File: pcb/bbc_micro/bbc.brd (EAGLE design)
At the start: 43 x 30 mm, 25 parts, among them U2 LM2776

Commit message: minor adjustment before production
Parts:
- moved U$4 6.15 mm to (20.0, 6.15)
- moved U$3 6.12 mm to (7.93, 5.80)
- moved C5 6.08 mm to (29.2, 2.56)
- moved J4 6.08 mm to (26.5, 22.3)
- moved U$5 6.08 mm to (26.3, 13.7)
- moved JP1 6.08 mm to (4.16, 1.83)
- moved C1 6.08 mm to (36.0, 13.1)
- moved C2 6.08 mm to (34.0, 20.3)
- moved C3 6.08 mm to (27.1, 8.65)
- moved C4 6.08 mm to (26.1, 2.56)
- moved C6 6.08 mm to (34.0, 13.1)
- moved C8 6.08 mm to (25.9, 10.7)
- moved C9 6.08 mm to (21.1, 16.4)
- moved JP3 6.08 mm to (33.3, 5.86)
- moved LED3 6.08 mm to (32.0, 13.1)
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
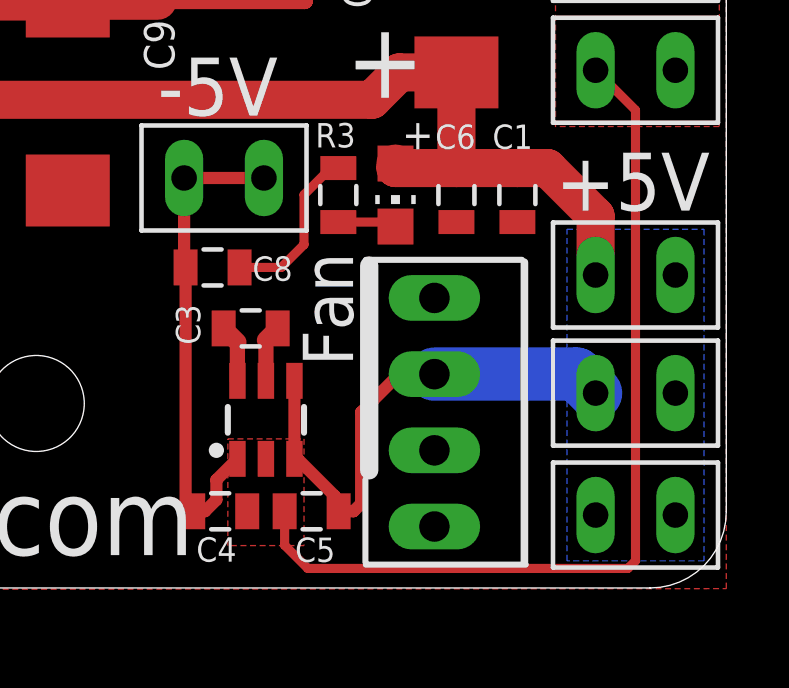
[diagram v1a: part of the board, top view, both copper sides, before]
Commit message: updated fan header
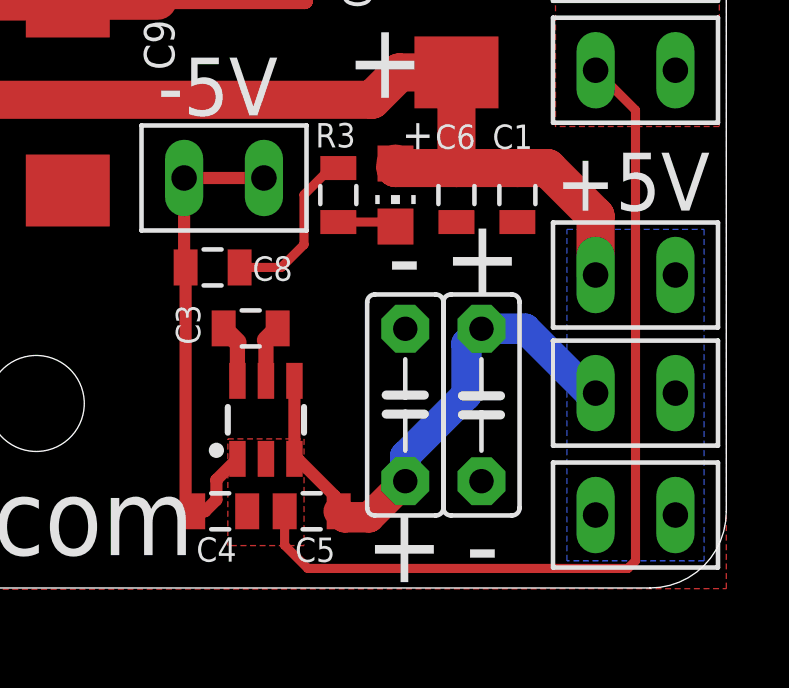
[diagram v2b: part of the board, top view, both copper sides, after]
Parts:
- removed JP3: (no value), appleii:1X04
- added C10, C16: (no value), capacitor-wima:C5B2.5
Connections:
- net +5V: now also C10.1, C16.1; no longer JP3.2
- net GND: now also C10.2, C16.2; no longer JP3.1
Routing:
- net +5V: track 70.0 -> 71.2 mm
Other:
- board text added: "-"
- board text removed: "Fan"
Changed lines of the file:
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@@
 <setting verticaltext="up"/>
 </settings>
-<grid distance="0.1" unitdist="mm" unit="mm" style="lines" multiple="1" display="no" altdistance="1" altunitdist="mil" altunit="mil"/>
+<grid distance="0.1" unitdist="mm" unit="mil" style="lines" multiple="1" display="no" altdistance="1" altunitdist="mil" altunit="mil"/>
 <layers>
 <layer number="1" name="Top" color="4" fill="1" visible="yes" active="yes"/>
@@
 <text x="36.2248" y="25.831" size="1.6764" layer="25" distance="35" rot="R90" align="center">GND</text>
 <rectangle x1="-1.395" y1="27.99" x2="12.605" y2="29.99" layer="51"/>
-<text x="29.721" y="9.287" size="1.6764" layer="25" distance="35" rot="R270" align="center">Fan</text>
 <text x="39.881" y="13.5442" size="1.9304" layer="25" distance="35" align="center">+5V</text>
 <text x="26.049" y="16.7138" size="1.9304" layer="25" distance="35" rot="R180" align="center">-5V</text>
@@
 <text x="31.626" y="17.6082" size="2.54" layer="25" distance="35" align="center">+</text>
 <text x="19.307" y="21.4182" size="2.54" layer="25" distance="35" align="center">+</text>
+<text x="32.271" y="1.465" size="2.54" layer="25" distance="35" align="center">+</text>
+<text x="34.871" y="1.465" size="2.54" layer="25" distance="35" align="center">-</text>
+<text x="34.871" y="11.065" size="2.54" layer="25" distance="35" align="center">+</text>
+<text x="32.271" y="11.065" size="2.54" layer="25" distance="35" align="center">-</text>
 </plain>
 <attributes>
@@
 <element name="U$4" library="a" package="M3_MOUNTING_HOLE_PACK" value="M3_MOUNTING_HOLE" x="20" y="6.15" smashed="yes"/>
 <element name="U$3" library="atx4vc" package="ROCK_SWITCH" value="ROCK_SW" x="7.93" y="5.8" smashed="yes"/>
-<element name="JP3" library="appleii" package="1X04" value="" x="33.271" y="5.858" smashed="yes" rot="R270"/>
 <element name="U$6" library="blade" package="2.8BLADE" value="BLADE28" x="39.974" y="10.432" smashed="yes"/>
 <element name="U$7" library="blade" package="2.8BLADE" value="BLADE28" x="39.974" y="6.495" smashed="yes"/>
@@
 <attribute name="SPICEPREFIX" value="C" x="21.051" y="16.399" size="1.778" layer="27" rot="R270" display="off"/>
 </element>
+<element name="C10" library="capacitor-wima" library_urn="urn:adsk.eagle:library:116" package="C5B2.5" package3d_urn="urn:adsk.eagle:package:5426/1" value="" x="34.84" y="6.1" smashed="yes" rot="R270">
+<attribute name="POPULARITY" value="10" x="34.84" y="6.1" size="1.778" layer="27" rot="R270" display="off"/>
+<attribute name="VALUE" x="32.046" y="8.132" size="1.27" layer="27" ratio="10" rot="R270"/>
+</element>
+<element name="C16" library="capacitor-wima" library_urn="urn:adsk.eagle:library:116" package="C5B2.5" package3d_urn="urn:adsk.eagle:package:5426/1" value="" x="32.3" y="6.1" smashed="yes" rot="R90">
+<attribute name="POPULARITY" value="10" x="32.3" y="6.1" size="1.778" layer="27" rot="R90" display="off"/>
+<attribute name="VALUE" x="35.094" y="4.068" size="1.27" layer="27" ratio="10" rot="R90"/>
+</element>
 </elements>
 <signals>
@@
 <vertex x="43" y="-0.022321875"/>
 </polygon>
-<contactref element="JP3" pad="1"/>
 <contactref element="U$9" pad="P$1"/>
 <contactref element="U$9" pad="P$2"/>
@@
 <wire x1="28.925" y1="11.446" x2="28.163" y2="10.684" width="0.3048" layer="1"/>
 <wire x1="28.163" y1="10.684" x2="26.777" y2="10.684" width="0.3048" layer="1"/>
+<contactref element="C10" pad="2"/>
+<contactref element="C16" pad="2"/>
 </signal>
 <signal name="+5V">
@@
 <contactref element="U$3" pad="P$4"/>
 <contactref element="C1" pad="2"/>
-<contactref element="JP3" pad="2"/>
 <contactref element="C6" pad="2"/>
 <contactref element="LED3" pad="A"/>
@@
 <wire x1="36.037" y1="13.997" x2="37.042" y2="13.997" width="1.27" layer="1"/>
 <wire x1="37.042" y1="13.997" x2="38.644" y2="12.395" width="1.27" layer="1"/>
-<wire x1="33.271" y1="7.128" x2="32.1" y2="7.128" width="0.4064" layer="1"/>
-<wire x1="30.83" y1="5.858" x2="32.1" y2="7.128" width="0.4064" layer="1"/>
 <wire x1="28.605" y1="4.3039" x2="28.7121" y2="4.3039" width="0.4064" layer="1"/>
 <wire x1="29.952" y1="3.064" x2="28.7121" y2="4.3039" width="0.4064" layer="1"/>
 <wire x1="29.952" y1="3.064" x2="29.952" y2="2.683" width="0.4064" layer="1"/>
 <wire x1="29.952" y1="2.683" x2="30.079" y2="2.556" width="0.4064" layer="1"/>
-<wire x1="30.83" y1="2.81" x2="30.576" y2="2.556" width="0.4064" layer="1"/>
-<wire x1="30.079" y1="2.556" x2="30.576" y2="2.556" width="0.4064" layer="1"/>
-<wire x1="30.83" y1="2.81" x2="30.83" y2="5.858" width="0.4064" layer="1"/>
 <wire x1="28.605" y1="4.3039" x2="28.605" y2="6.9041" width="0.4064" layer="1"/>
 <contactref element="C2" pad="+"/>
@@
 <wire x1="17.328" y1="16.272" x2="31.186" y2="16.272" width="1.27" layer="1"/>
 <wire x1="34.005" y1="13.997" x2="34.005" y2="17.186" width="1.27" layer="1"/>
-<wire x1="33.271" y1="7.128" x2="38.011" y2="7.128" width="1.778" layer="16"/>
-<wire x1="38.011" y1="7.128" x2="38.644" y2="6.495" width="1.778" layer="16"/>
 <polygon width="0.1524" layer="16" thermals="no">
 <vertex x="37.688" y="11.954"/>
@@
 <vertex x="37.688" y="0.905"/>
 </polygon>
+<contactref element="C10" pad="1"/>
+<contactref element="C16" pad="1"/>
+<wire x1="34.84" y1="8.64" x2="36.299" y2="8.64" width="1.016" layer="16"/>
+<wire x1="38.444" y1="6.495" x2="36.299" y2="8.64" width="1.016" layer="16"/>
+<wire x1="38.444" y1="6.495" x2="38.644" y2="6.495" width="1.016" layer="16"/>
+<wire x1="34.84" y1="8.64" x2="34.34" y2="8.14" width="1.016" layer="16"/>
+<wire x1="34.34" y1="8.14" x2="34.34" y2="6.44" width="1.016" layer="16"/>
+<wire x1="32.3" y1="4.4" x2="32.3" y2="3.56" width="1.016" layer="16"/>
+<wire x1="34.34" y1="6.44" x2="32.3" y2="4.4" width="1.016" layer="16"/>
+<wire x1="30.079" y1="2.556" x2="30.279" y2="2.356" width="1.016" layer="1"/>
+<wire x1="31.096" y1="2.356" x2="30.279" y2="2.356" width="1.016" layer="1"/>
+<wire x1="31.096" y1="2.356" x2="32.3" y2="3.56" width="1.016" layer="1"/>
 </signal>
 <signal name="N$31">
